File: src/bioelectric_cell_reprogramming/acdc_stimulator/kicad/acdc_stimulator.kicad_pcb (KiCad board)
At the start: 4 copper layers, 139 x 133 mm, 145 parts, among them IC1 AD9833BRM-REEL7, IC2 AD5122BCPZ10-RL7, IC3 LTC3896EFE#PBF, IC4 LTC3637IMSE#PBF, IC5 LTC3637IMSE#PBF, IC6 LTC3637IMSE#PBF, J1 Screw_Terminal_01x02, J2 Conn_ARM_SWD_TagConnect_TC203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, J3 USB_C_Receptacle_USB2.0_14P, J4 S4B-PH-SM4-TB, J5 IPL1-102-01-L-S-K, J6 Screw_Terminal_01x02, J7 IPL1-102-01-L-S-K, J8 6620XX11122_66200211122, J9 6620XX11122_66200211122, Q1 BSZ096N10LS5ATMA1, Q10 BSZ096N10LS5ATMA1, Q11 BSZ096N10LS5ATMA1, Q2 NDT3055L, Q3 BSC520N15NS3G, Q4 BSC520N15NS3G, Q5 IPD320N20N3GATMA1, Q6 BSZ096N10LS5ATMA1, Q7 BSZ096N10LS5ATMA1, Q8 IPB320P10LMATMA1, Q9 IPB320P10LMATMA1, SW1 SW_Push, SW2 SW_SPDT, U1 STM32G473RCTx, U2 AMS1117-3.3, U3 USBLC6-2SC6, U4 LTC6090CFE-PBF, U5 LTC6090CFE-PBF, U7 DRV8873HPWPR, Y1 16Mhz

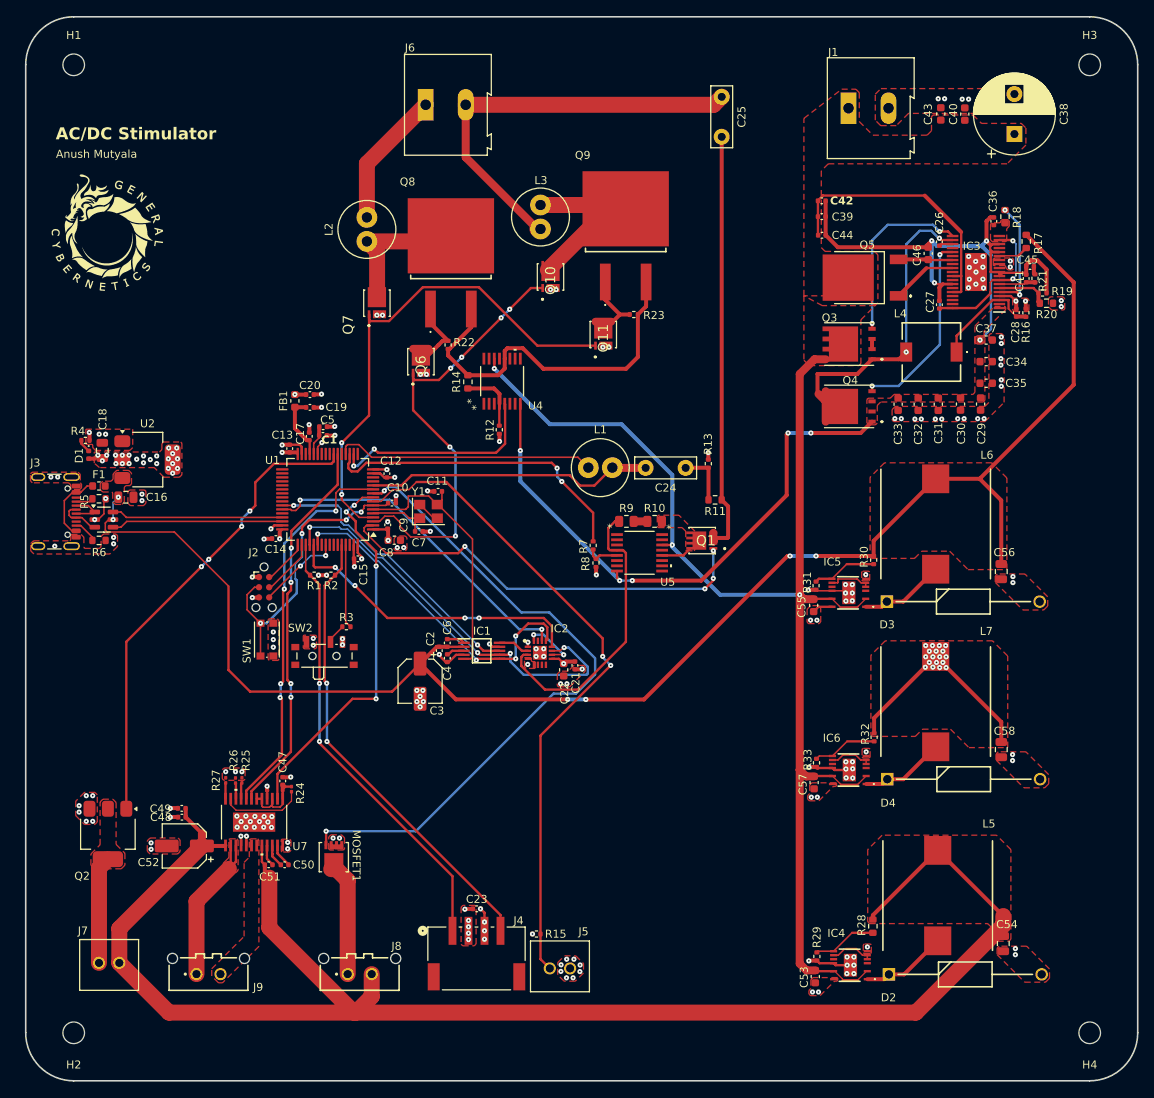
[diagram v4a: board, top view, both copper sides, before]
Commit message: fixed some more clearance errors
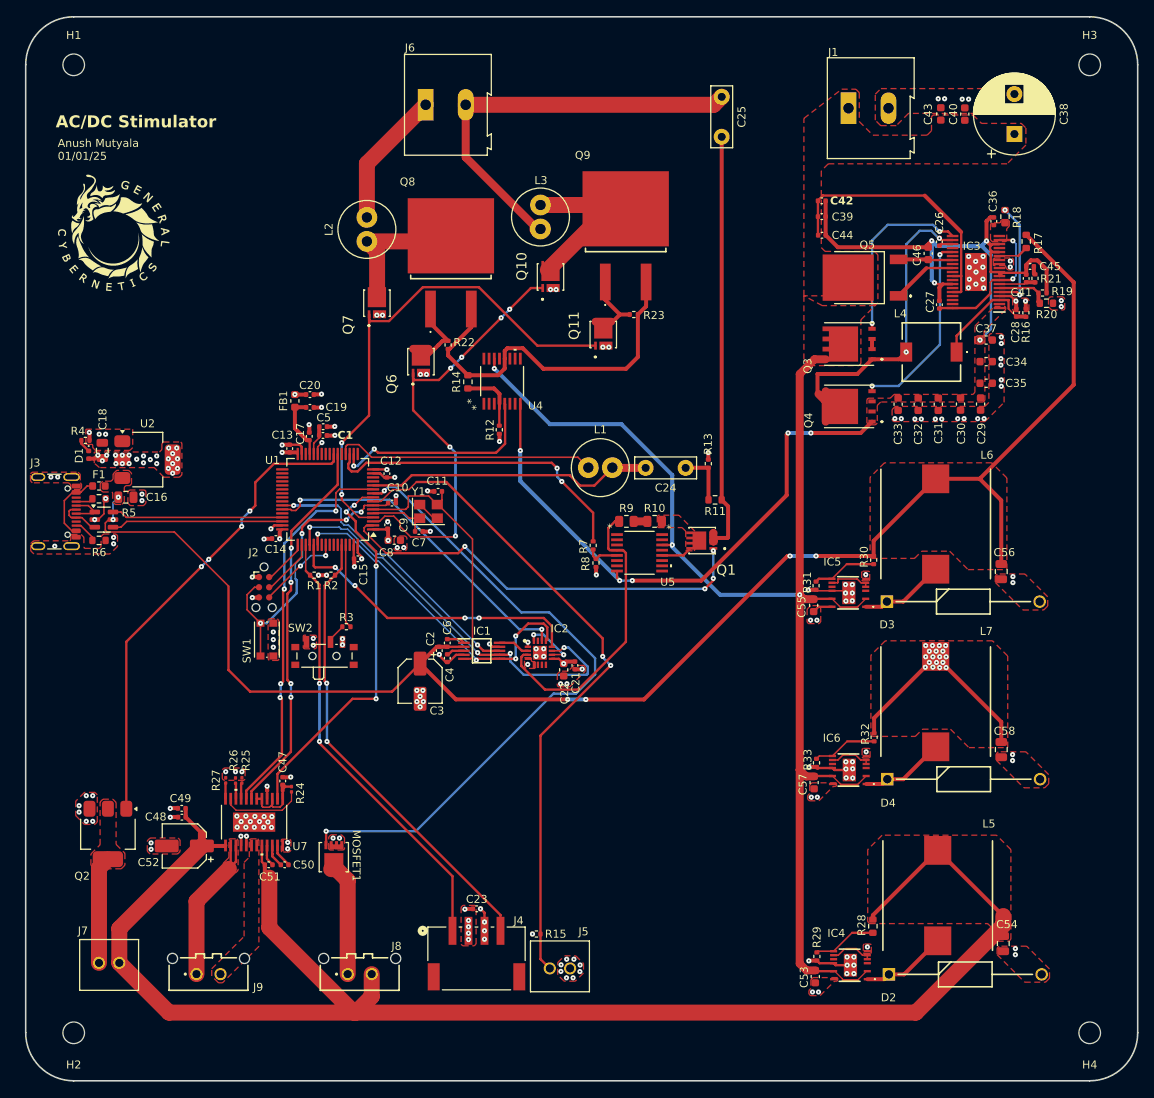
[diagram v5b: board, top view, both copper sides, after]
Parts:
- moved G*** 0.80 mm to (82.0, 48.0)
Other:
- board text added: "Anush Mutyala 01/01/25"
- board text removed: "Anush Mutyala"
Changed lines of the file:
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@@
 		)
 		(pad "2" smd roundrect
-			(at 0.32 0 270)
-			(size 0.46 0.4)
+			(at 0.34 0 270)
+			(size 0.44 0.4)
 			(layers "F.Cu" "F.Mask")
 			(roundrect_rratio 0.25)
@@
 		(tags "capacitor")
 		(property "Reference" "C4"
-			(at -1.88 0 90)
+			(at -2.08 0.3 90)
 			(layer "F.SilkS")
 			(effects
@@
 		(tags "capacitor")
 		(property "Reference" "C45"
-			(at 0.3425 0.83 0)
+			(at -2.5075 0.005 0)
 			(layer "F.SilkS")
 			(effects
@@
 		(tags "resistor")
 		(property "Reference" "R21"
-			(at -0.305 0.9875 -90)
+			(at -0.055 1.9875 0)
 			(layer "F.SilkS")
 			(effects
@@
 		(tags "MOSFET (N-Channel)")
 		(property "Reference" "Q1"
-			(at 0.173 0 180)
+			(at -2.3575 -3.67464 180)
 			(layer "F.SilkS")
 			(effects
@@
 		(tags "capacitor")
 		(property "Reference" "C5"
-			(at 0.5425 -0.86 0)
+			(at 0.0675 -1.135 0)
 			(layer "F.SilkS")
 			(effects
@@
 		(tags "MOSFET (N-Channel)")
 		(property "Reference" "Q11"
-			(at 0.173 0 90)
+			(at 1.745 -3.65 90)
 			(layer "F.SilkS")
 			(effects
@@
 		(tags "capacitor")
 		(property "Reference" "C41"
-			(at -0.32 -0.8375 90)
+			(at -1.745 -0.6125 0)
 			(layer "F.SilkS")
 			(effects
@@
 		(tags "MOSFET (N-Channel)")
 		(property "Reference" "Q10"
-			(at 0.173 0 90)
+			(at 1.945 -3.6 90)
 			(layer "F.SilkS")
 			(effects
@@
 		(tags "capacitor")
 		(property "Reference" "C48"
-			(at 2.625 -0.0055 0)
+			(at 3.275 0.0445 0)
 			(layer "F.SilkS")
 			(effects
@@
 		)
 		(pad "2" smd roundrect
-			(at 0.32 0 270)
-			(size 0.46 0.4)
+			(at 0.34 0 270)
+			(size 0.44 0.4)
 			(layers "F.Cu" "F.Mask")
 			(roundrect_rratio 0.25)
@@
 		)
 		(pad "2" smd roundrect
-			(at 0.32 0 270)
-			(size 0.46 0.4)
+			(at 0.34 0 270)
+			(size 0.44 0.4)
 			(layers "F.Cu" "F.Mask")
 			(roundrect_rratio 0.25)
@@
 		(tags "resistor")
 		(property "Reference" "R5"
-			(at -1.8125 0.35 90)
+			(at 3.7375 1.75 180)
 			(layer "F.SilkS")
 			(effects
@@
 		(tags "MOSFET (N-Channel)")
 		(property "Reference" "Q4"
-			(at 3.255 0.15 180)
+			(at -1.745 -5.075 -90)
 			(layer "F.SilkS")
 			(effects
@@
 		(tags "capacitor")
 		(property "Reference" "C49"
-			(at 2.655 -0.0555 0)
+			(at 0.155 1.2445 0)
 			(layer "F.SilkS")
 			(effects
@@
 	(footprint "LOGO"
 		(layer "F.Cu")
-		(at 81.2 47.975)
+		(at 82 48)
 		(property "Reference" "G***"
 			(at 0 0 0)
@@
 		)
 		(pad "2" smd roundrect
-			(at 0.32 0 270)
-			(size 0.46 0.4)
+			(at 0.34 0 270)
+			(size 0.44 0.4)
 			(layers "F.Cu" "F.Mask")
 			(roundrect_rratio 0.25)
@@
 		(tags "MOSFET (N-Channel)")
 		(property "Reference" "Q6"
-			(at 0.173 0 90)
+			(at -2.165 -3.65 90)
 			(layer "F.SilkS")
 			(effects
@@
 		(tags "capacitor")
 		(property "Reference" "C1"
-			(at 0.785 0.54 0)
+			(at 2.7875 -0.035 0)
 			(layer "F.SilkS")
 			(effects
@@
 		(tags "MOSFET (N-Channel)")
 		(property "Reference" "Q3"
-			(at 3.28 -2.45 180)
+			(at -2.745 -5.175 -90)
 			(layer "F.SilkS")
 			(effects
@@
 	)
 	(gr_text "AC/DC Stimulator"
-		(at 74.75 36.5 0)
+		(at 74.75 35 0)
 		(layer "F.SilkS")
 		(effects
@@
 		)
 	)
-	(gr_text "Anush Mutyala\n"
-		(at 74.775 38.75 0)
+	(gr_text "Anush Mutyala\n01/01/25"
+		(at 75 39 0)
 		(layer "F.SilkS")
 		(effects
@@
 	)
 	(segment
-		(start 97.925 116.8595)
+		(start 97.925 116.8795)
+		(end 98.025 116.7795)
+		(width 0.3)
+		(layer "F.Cu")
+		(net 135)
+	)
+	(segment
+		(start 98.025 116.7795)
 		(end 98.025 116.7595)
 		(width 0.3)
@@
 	(segment
 		(start 97.925 118.7445)
-		(end 97.925 116.8595)
+		(end 97.925 116.8795)
 		(width 0.3)
 		(layer "F.Cu")

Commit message: ci: replaced digital pot with one thats available in JLCPCB
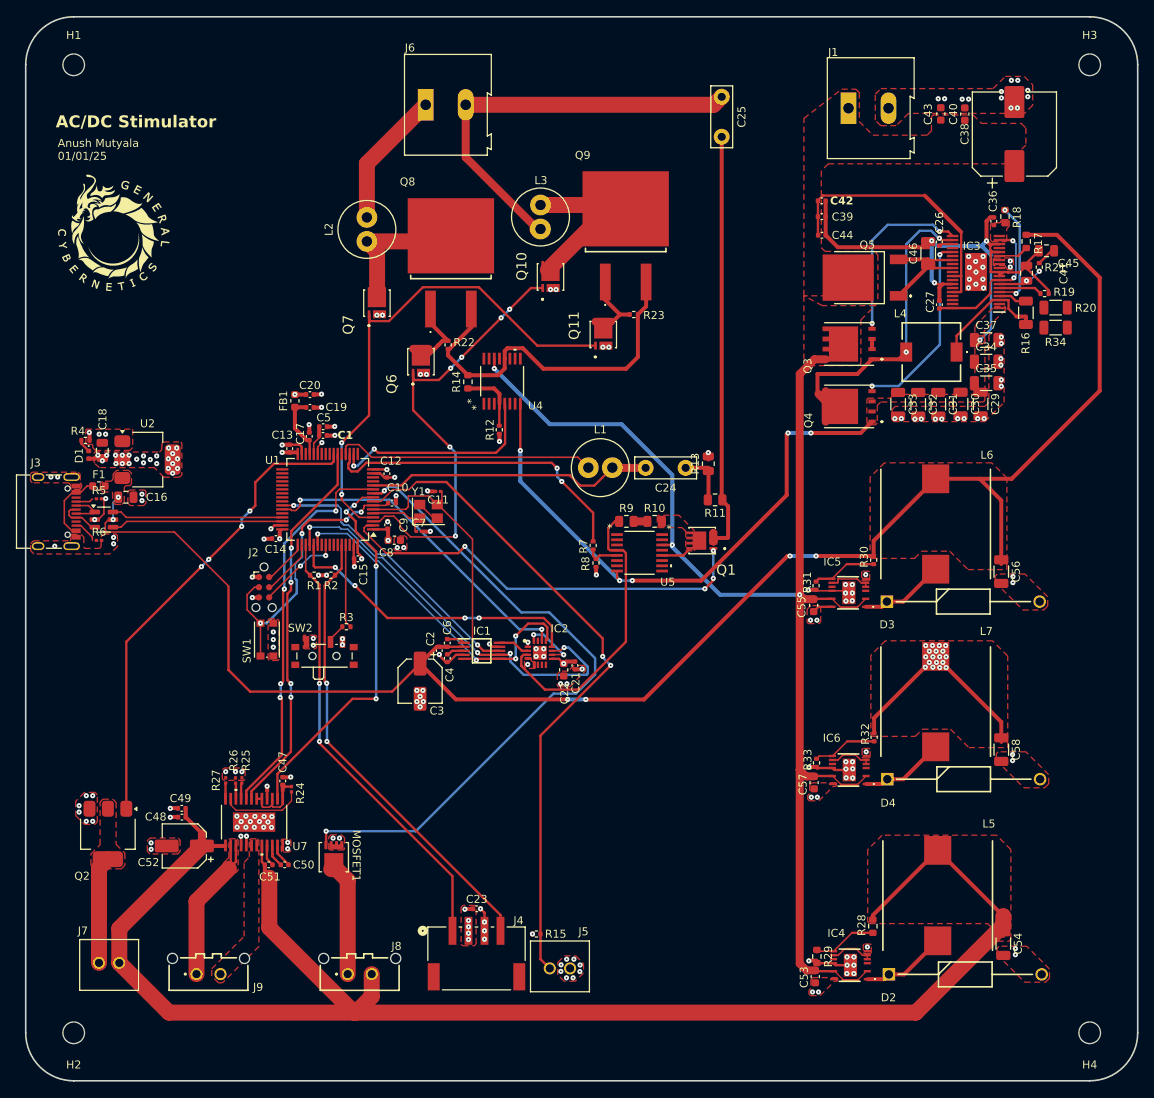
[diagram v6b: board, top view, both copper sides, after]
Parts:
- removed C28: 1n, Capacitor_SMD:C_0402_1005Metric
- added R34: 370k, Resistor_SMD:R_1206_3216Metric, F.Cu at (199.7, 59.9)
- C11, C7: value 30p -> 10p; footprint Capacitor_SMD:C_0402_1005Metric -> Capacitor_SMD:C_0201_0603Metric
- C24, C25: value 100u -> 0
- C29, C30, C31, C32, C33, C34, C35, C37, C46: footprint Capacitor_SMD:C_0603_1608Metric -> Capacitor_SMD:C_1206_3216Metric
- C38: footprint Capacitor_THT:CP_Radial_D10.0mm_P5.00mm -> Capacitor_SMD:CP_Elec_10x10
- C41, C45: footprint Capacitor_SMD:C_0402_1005Metric -> Capacitor_SMD:C_0805_2012Metric
- C54, C56, C58: footprint Capacitor_SMD:C_0805_2012Metric -> Capacitor_SMD:C_1206_3216Metric
- J3: footprint Connector_USB:USB_C_Receptacle_GCT_USB4105-xx-A_16P_TopMnt_Horizontal -> Connector_USB:USB_C_Receptacle_XKB_U262-16XN-4BVC11
- L1, L2, L3: value 2.5 -> 0
- R11: value 1M -> 10k; footprint Resistor_SMD:R_0603_1608Metric -> Resistor_SMD:R_0805_2012Metric
- R13: value 10k -> 100; footprint Resistor_SMD:R_0402_1005Metric -> Resistor_SMD:R_0805_2012Metric
- R16: footprint Resistor_SMD:R_0402_1005Metric -> Resistor_SMD:R_1206_3216Metric
- R20: value 740k -> 370k; footprint Resistor_SMD:R_0603_1608Metric -> Resistor_SMD:R_1206_3216Metric
- R29: footprint Resistor_SMD:R_0402_1005Metric -> Resistor_SMD:R_0603_1608Metric
- R30: value 42.5k -> 17.8k
- R32: value 31.25k -> 8.2k
- R5, R6: footprint Resistor_SMD:R_0603_1608Metric -> Resistor_SMD:R_0201_0603Metric
- moved C45 2.84 mm to (198.6, 50.2)
- moved R21 1.50 mm to (197.7, 52.3)
- moved R20 1.27 mm to (199.7, 57.4)
- moved C41 0.66 mm to (196.1, 53.0)
- moved R19 0.27 mm to (198.4, 55.6)
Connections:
- Q1 pad 10: /V_AC -> (no net)
- Q1 pad 11: /V_AC -> (no net)
- Q1 pad 9: /LTC6090_AC/OUT -> (no net)
- Q10 pad 10: GND -> (no net)
- Q10 pad 11: GND -> (no net)
- Q10 pad 9: /V_DC2 -> (no net)
- Q11 pad 10: GND -> (no net)
- Q11 pad 11: GND -> (no net)
- Q11 pad 9: Net-(Q11-D_1) -> (no net)
- Q4 pad 5: /DCDC_inverter/SW -> Net-(Q4-D_1)
- Q4 pad 7: /DCDC_inverter/SW -> Net-(Q4-D_1)
- Q4 pad 8: /DCDC_inverter/SW -> Net-(Q4-D_1)
- Q4 pad 9: /DCDC_inverter/SW -> Net-(Q4-D_1)
- Q6 pad 10: GND -> (no net)
- Q6 pad 11: GND -> (no net)
- Q6 pad 9: Net-(Q6-D_1) -> (no net)
- Q7 pad 10: GND -> (no net)
- Q7 pad 11: GND -> (no net)
- Q7 pad 9: /V_DC1 -> (no net)
- R20 pad 2: GND -> Net-(R20-Pad2)
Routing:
- net +5V: track 200.7 -> 208.0 mm
- net Net-(C45-Pad1): track 1.04 -> 2.48 mm
- net /DCDC_inverter/ITH: track 4.55 -> 5.65 mm, vias 0 -> 2
- net /DCDC_inverter/VFB: track 6.49 -> 5.43 mm
- net /DCDC_inverter/SENSE+: track 14.1 -> 15.0 mm
- net GND: track 65.8 -> 65.1 mm, vias 192 -> 188

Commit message: ci: fixed all relevant DRC errors with new components
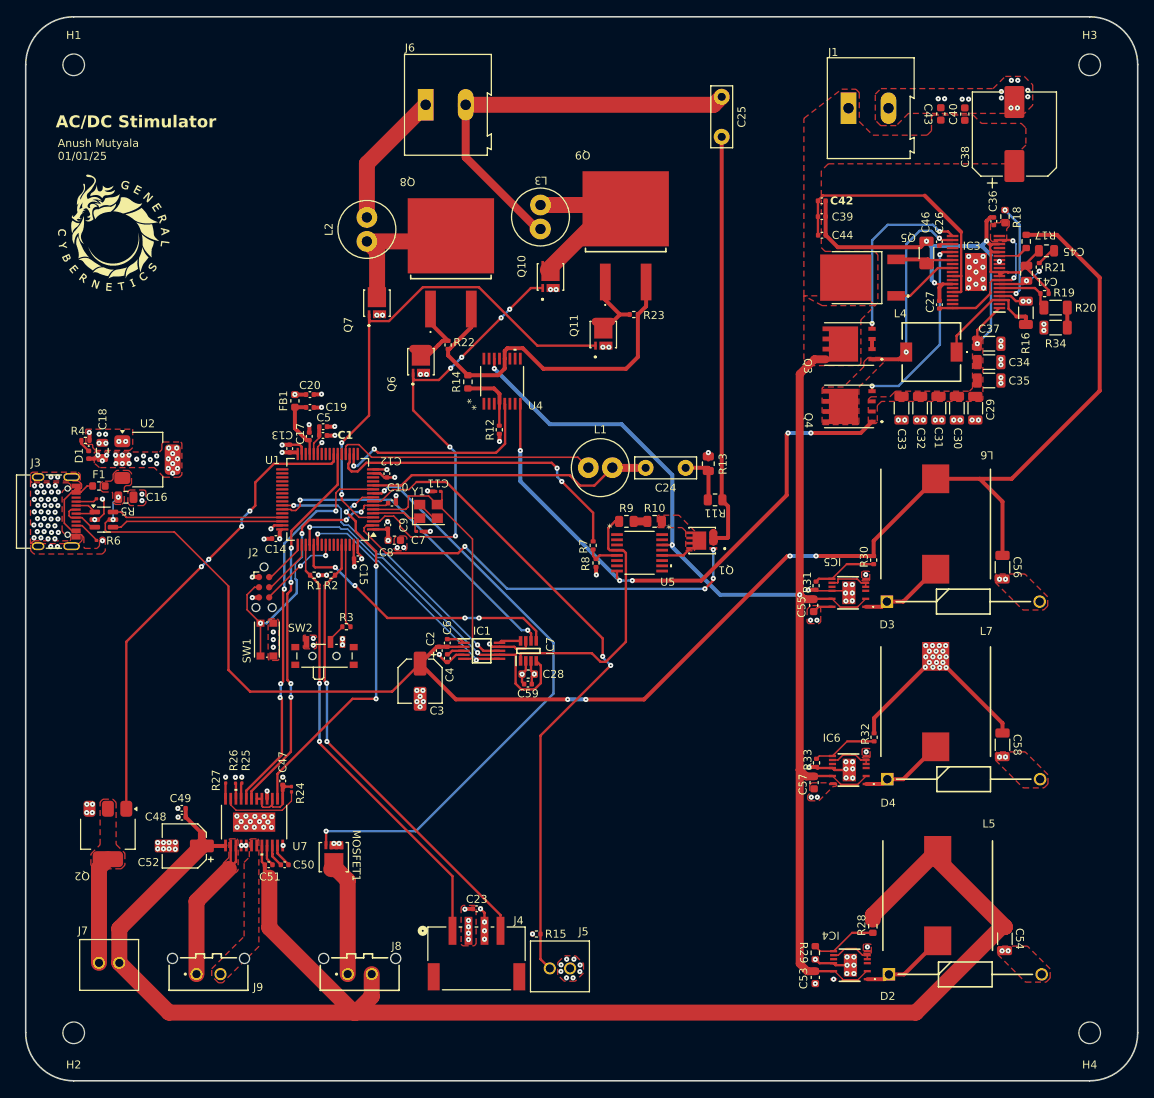
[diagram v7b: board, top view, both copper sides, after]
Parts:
- removed C21: 0.1u, Capacitor_SMD:C_0402_1005Metric
- removed C22: 10u, Capacitor_SMD:C_0603_1608Metric
- removed IC2: AD5122BCPZ10-RL7, AD5122BCPZ10-RL7:QFN50P300X300X80-17N-D
- added C28: 10u, Capacitor_SMD:C_0603_1608Metric, F.Cu at (133.8, 103.2)
- added C59: 0.1u, Capacitor_SMD:C_0402_1005Metric, F.Cu at (133.8, 104.4)
- added IC7: AD5160BRJZ10-RL7, AD5160BRJZ10-RL7:SOT65P280X145-8N, F.Cu at (133.8, 100.3)
- moved C29 0.84 mm to (189.7, 69.9)
- moved C30 0.69 mm to (187.4, 69.9)
- moved C33 0.65 mm to (180.5, 69.9)
- moved C54 0.63 mm to (193.4, 136.2)
- moved C58 0.62 mm to (193.1, 112.0)
- moved C37 0.59 mm to (191.4, 61.9)
- moved C56 0.57 mm to (193.1, 89.8)
- moved C32 0.55 mm to (182.8, 69.9)
- moved R29 0.50 mm to (169.7, 138.0)
- moved C35 0.50 mm to (191.4, 66.5)
- moved C31 0.50 mm to (185.1, 69.9)
- moved C34 0.37 mm to (191.4, 64.2)
- moved Q5 0.31 mm to (170.3, 53.6)
- moved C46 0.22 mm to (183.6, 50.5)
- moved C53 0.10 mm to (169.7, 141.1)
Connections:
- Q4 pad 5: Net-(Q4-D_1) -> /DCDC_inverter/SW
- Q4 pad 7: Net-(Q4-D_1) -> /DCDC_inverter/SW
- Q4 pad 8: Net-(Q4-D_1) -> /DCDC_inverter/SW
- Q4 pad 9: Net-(Q4-D_1) -> /DCDC_inverter/SW
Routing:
- net /DCDC_inverter/SW: track 40.4 -> 25.2 mm
- net /SPI_DO: track 42.2 -> 30.8 mm, vias 4 -> 2
- net /INCUBATOR_PELT_OUT: track 82.5 -> 74.8 mm
- net Net-(IC2-VLOGIC): track 7.06 -> 0.00 mm, vias 2 -> 0
- net /SPI_CLK: track 51.9 -> 44.9 mm, vias 4 -> 2
- net -60V: track 147.5 -> 153.7 mm
- net /POT_OUT: track 36.6 -> 33.4 mm
- net /SPI_DI: track 38.1 -> 35.1 mm
- net Net-(R20-Pad2): track 0.00 -> 2.50 mm
- net +12V: track 203.7 -> 201.7 mm
- net /DCDC_inverter/VFB: track 5.43 -> 7.35 mm
- net /POT_CS: track 41.6 -> 40.0 mm
- net /FG_OUT: track 3.96 -> 2.74 mm
- net +3.3V: track 48.0 -> 46.9 mm
- net +5V: track 208.0 -> 207.0 mm
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- added copper zone on F.Cu, net /DCDC_inverter/SW
- removed copper zone on F.Cu, net +12V
